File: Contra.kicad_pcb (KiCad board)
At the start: 2 copper layers, 231 x 76.2 mm, 110 parts, among them P1 Pad, P2 Pad, P3 Pad, P4 Pad, SW1 SW_PUSH, U1 ProMicro

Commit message: Repair the mess of questionable routing decisions
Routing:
- net ROW3: track 269.8 -> 265.7 mm
- net GND: track 93.6 -> 89.8 mm
- net Net-(SW1-Pad1): track 58.8 -> 56.3 mm
- net COL2: track 74.0 -> 72.1 mm
- net ROW0: track 270.5 -> 268.8 mm
- net COL1: track 75.3 -> 73.8 mm
- net +5V: track 77.4 -> 76.2 mm, vias 1 -> 0
- net COL0: track 105.3 -> 106.4 mm
- net COL11: track 232.1 -> 231.4 mm
- net ROW2: track 222.0 -> 221.4 mm
- net Net-(D35-Pad2): track 17.3 -> 16.7 mm
- net Net-(P2-Pad1): track 42.7 -> 43.2 mm
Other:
- net class Power added: clearance 0.2, trace_width 0.381, via_dia 0.6, via_drill 0.4

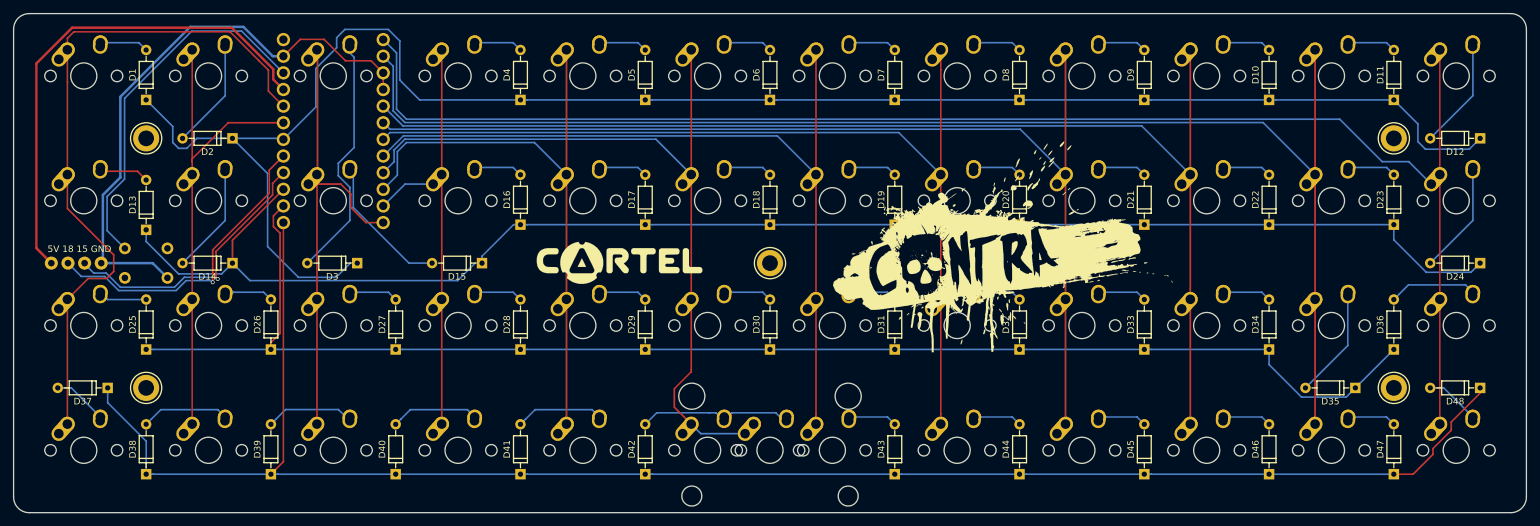
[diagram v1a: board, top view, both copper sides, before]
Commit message: Convert to KiCad 5
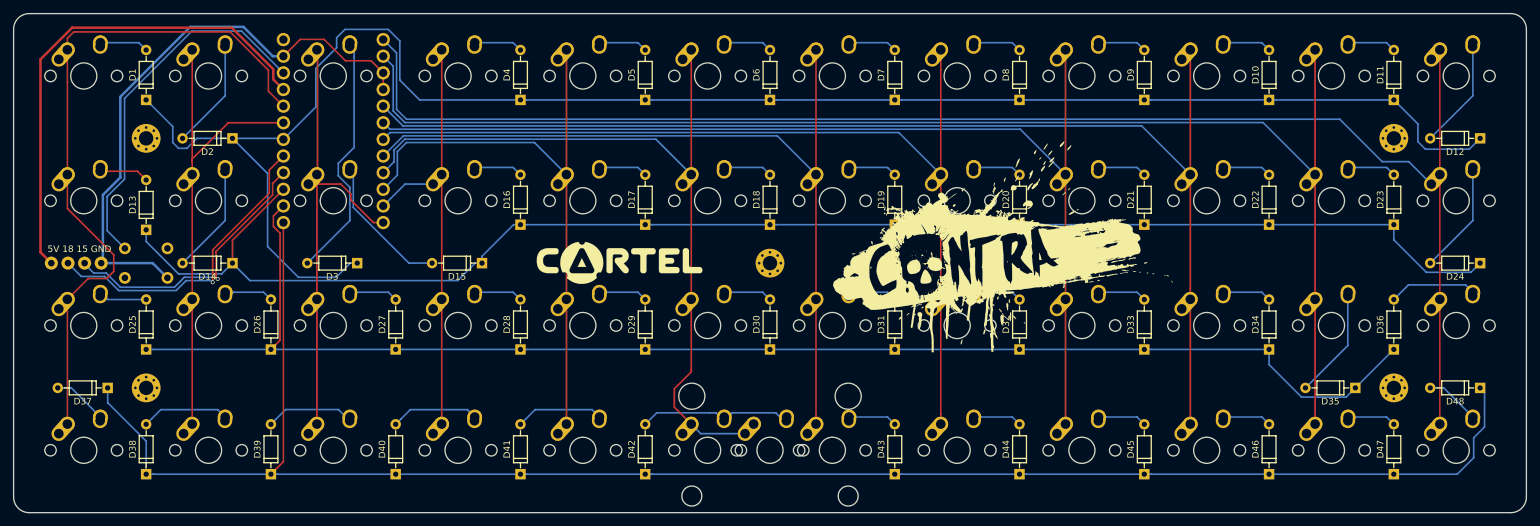
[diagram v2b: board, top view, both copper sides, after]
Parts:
- removed the REF** at (47.6, 47.6)
- removed the REF** at (238.1, 47.6)
- removed the REF** at (47.6, 85.7)
- removed the REF** at (238.1, 85.7)
- removed the REF** at (142.9, 66.7)
- added REF**: MountingHole_2.2mm_M2_Pad_Via, Mounting_Holes:MountingHole_2.2mm_M2_Pad_Via, F.Cu at (238.1, 85.7)
- added REF**: MountingHole_2.2mm_M2_Pad_Via, Mounting_Holes:MountingHole_2.2mm_M2_Pad_Via, F.Cu at (238.1, 47.6)
- added REF**: MountingHole_2.2mm_M2_Pad_Via, Mounting_Holes:MountingHole_2.2mm_M2_Pad_Via, F.Cu at (142.9, 66.7)
- added REF**: MountingHole_2.2mm_M2_Pad_Via, Mounting_Holes:MountingHole_2.2mm_M2_Pad_Via, F.Cu at (47.6, 47.6)
- added REF**: MountingHole_2.2mm_M2_Pad_Via, Mounting_Holes:MountingHole_2.2mm_M2_Pad_Via, F.Cu at (47.6, 85.7)
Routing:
- net ROW3: track 265.7 -> 270.2 mm
- net Net-(D3-Pad2): track 38.4 -> 39.4 mm
- net COL2: track 72.1 -> 71.4 mm
- net +5V: track 76.2 -> 75.7 mm
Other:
- board text removed: "+5V"

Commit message: Update gerbers
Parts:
- removed P1, P2, P3, P4: Pad, locallib:mountinghole
- added G***: LOGO, locallib:ai-ring-6mm-FancyAss, B.Cu at (228.6, 65.1)
- added G***: LOGO, locallib:ai-ring-6mm-FancyAss-Mask, B.Cu at (228.6, 65.1)
- added G***: LOGO, locallib:ai-ring-6mm, F.Cu at (253.2, 100.0)
- added J1: Conn_01x04, Pin_Headers:Pin_Header_Straight_1x04_Pitch2.54mm, F.Cu at (41.9, 66.7)
- D1, D10, D11, D12, D13, D14, D15, D16, D17, D18, D19, D2, D20, D21, D22, D23, D24, D25, D26, D27, D28, D29, D3, D30, D31, D32, D33, D34, D35, D36, D37, D38, D39, D4, D40, D41, D42, D43, D44, D45, D46, D47, D48, D5, D6, D7, D8, D9: footprint Diodes_THT:D_DO-35_SOD27_P7.62mm_Horizontal -> locallib:D_DO-35_SOD27_P7.62mm_Horizontal-DoubleSided
- SW1: footprint Molex-0548190589:PushButton_6x6mm_TH -> Molex-0548190589:PushButton_6x6mm_TH_Pretty
- moved D13 15.0 mm to (42.1, 47.6), turned to 180 degrees
- moved D25 14.7 mm to (61.1, 85.7), turned to 180 degrees
- turned SW1 to 90 degrees
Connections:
- U1 pad 16: Net-(P2-Pad1) -> PIN15
- U1 pad 17: Net-(P1-Pad1) -> PIN18
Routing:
- net Net-(P1-Pad1): track 48.3 -> 0.00 mm, vias 1 -> 0
- net PIN18: track 0.00 -> 48.1 mm, vias 0 -> 1
- net PIN15: track 0.00 -> 43.3 mm, vias 0 -> 1
- net Net-(P2-Pad1): track 43.2 -> 0.00 mm, vias 1 -> 0
- net ROW1: track 232.9 -> 249.2 mm
- net Net-(D25-Pad2): track 7.45 -> 20.0 mm
- net ROW2: track 221.4 -> 210.5 mm
- net COL0: track 106.4 -> 109.6 mm
- net GND: track 89.8 -> 87.3 mm
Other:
- board text added: "+5V"
- board text added: "15"
- board text added: "18"
- board text added: "Contra PCB by ai03 Revision 2.0"
- board text added: "GND"
- board text added: "Pro Micro here! Component side faces away from the PCB."
- board text removed: "5V 18 15 GND"
- board text removed: "Pro Micro here! Component side faces away from the PCB. Rev 2.0"
